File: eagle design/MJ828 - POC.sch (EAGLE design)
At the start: 34 parts, among them IC1 ATTINY4313-MMH, IC2 PRQV8.00CR1510Y00L, IC3 MCP2515, IC5 MCP2561-2, IC6 LDK320ADU50R, SW1 6x6mm spst-no tact, SW2 6x6mm spst-no tact, X1 CAN, X2 BAT

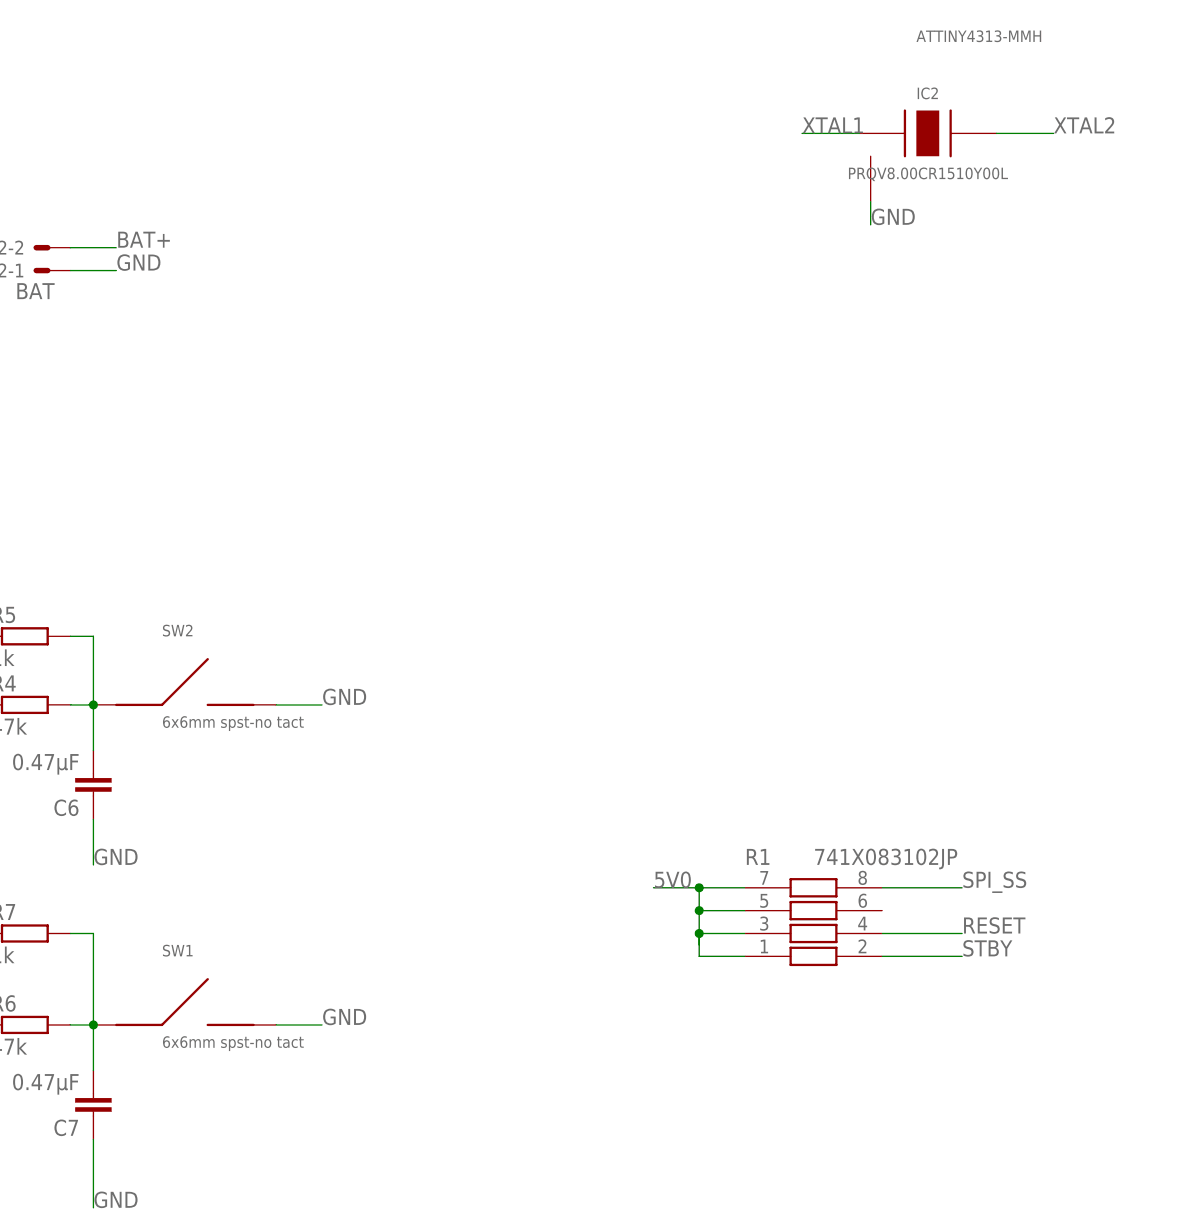
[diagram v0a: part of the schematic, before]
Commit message: - replaced oscillator, fet and mj808 utility led with better components, updated schematics - added/removed relevant datasheets for above changes
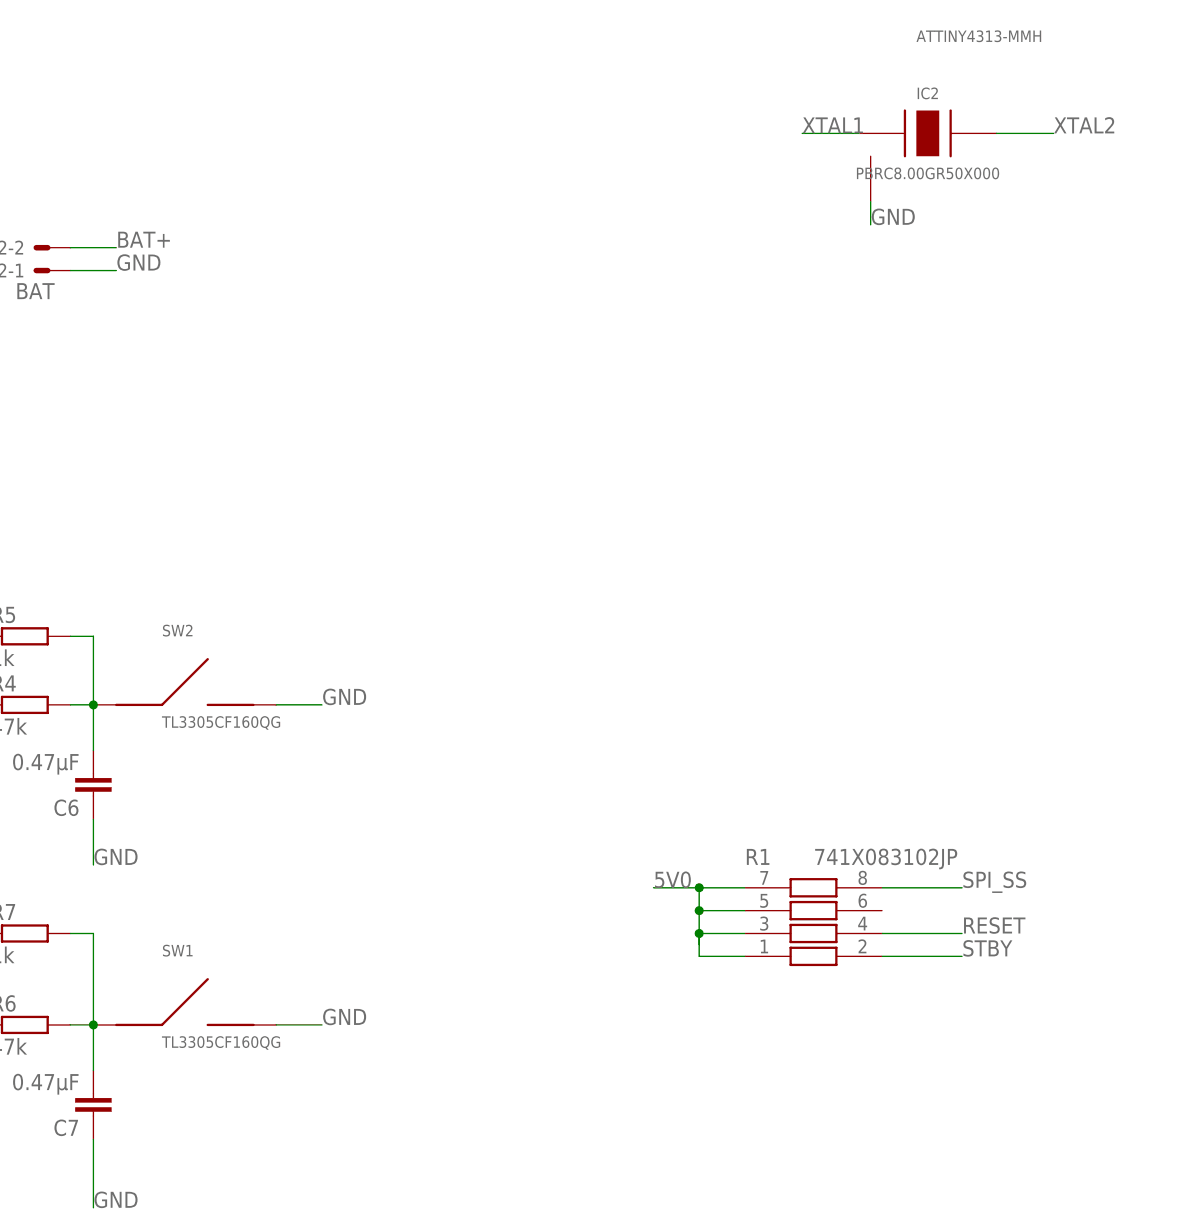
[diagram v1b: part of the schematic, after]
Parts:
- IC2: value PRQV8.00CR1510Y00L -> PBRC8.00GR50X000
- SW1, SW2: value 6x6mm spst-no tact -> TL3305CF160QG
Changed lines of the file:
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@@
 <attribute name="SPICEPREFIX" value="X"/>
 </part>
-<part name="IC2" library="PRQV8.00CR1510Y00L - 8MHz resonator" deviceset="PRQV" device="" value="PRQV8.00CR1510Y00L"/>
+<part name="IC2" library="PRQV8.00CR1510Y00L - 8MHz resonator" deviceset="PRQV" device="" value="PBRC8.00GR50X000"/>
 <part name="C3" library="rcl" library_urn="urn:adsk.eagle:library:334" deviceset="C-EU" device="C0402" package3d_urn="urn:adsk.eagle:package:23626/2" value="1μF"/>
 <part name="C4" library="rcl" library_urn="urn:adsk.eagle:library:334" deviceset="C-EU" device="C0402" package3d_urn="urn:adsk.eagle:package:23626/2" value="1μF"/>
@@
 <part name="R2" library="741X083331JP Resistor Array" deviceset="741X083331JP" device="" value="741X083331JP"/>
 <part name="R1" library="741X083331JP Resistor Array" deviceset="741X083331JP" device="" value="741X083102JP"/>
-<part name="SW2" library="TL3305-844809 SPST-NO Tact Switch" deviceset="TL3305-844809" device="" value="6x6mm spst-no tact"/>
-<part name="SW1" library="TL3305-844809 SPST-NO Tact Switch" deviceset="TL3305-844809" device="" value="6x6mm spst-no tact"/>
+<part name="SW2" library="TL3305-844809 SPST-NO Tact Switch" deviceset="TL3305-844809" device="" value="TL3305CF160QG"/>
+<part name="SW1" library="TL3305-844809 SPST-NO Tact Switch" deviceset="TL3305-844809" device="" value="TL3305CF160QG"/>
 <part name="R3" library="741X083331JP Resistor Array" deviceset="741X083331JP" device="" value="741X083102JP"/>
 <part name="C6" library="rcl" library_urn="urn:adsk.eagle:library:334" deviceset="C-EU" device="C0402" package3d_urn="urn:adsk.eagle:package:23626/2" value="0.47μF"/>
